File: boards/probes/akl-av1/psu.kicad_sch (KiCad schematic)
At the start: 15 parts, among them J1 U.FL, U1 LTC1983-5, U2 ADP7142ACPZN-R7, U3 ADP7182_DFN8

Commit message: Rev 0.2 of AKL-AV1
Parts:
- added L1: FERRITE, azonenberg_pcb:EIA_0402_CAP_NOSILK, symbol passive-azonenberg:INDUCTOR_PWROUT
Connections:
- net 5V0_N: now also L1.2; no longer C7.1, U1.2 (VOUT)
- new net: C7.1, L1.1, U1.2 (VOUT)
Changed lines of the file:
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@@
 (kicad_sch (version 20211123) (generator eeschema)
   (paper "A4")
+  (junction (at 72.39 26.67) (diameter 0) (color 0 0 0 0)
+  )
   (junction (at 34.29 99.06) (diameter 0) (color 0 0 0 0)
   )
@@
     (effects (font (size 1.27 1.27)) (justify left bottom))
   )
-  (label "5V0_N" (at 72.39 26.67 0)
+  (label "5V0_N" (at 87.63 26.67 0)
     (effects (font (size 1.27 1.27)) (justify left bottom))
   )
@@
     )
     (pin "1")
+    (pin "2")
+  )
+  (symbol (lib_id "passive-azonenberg:INDUCTOR_PWROUT") (at 80.01 26.67 90) (unit 1)
+    (in_bom yes) (on_board yes) (fields_autoplaced)
+    (property "Reference" "L1" (id 0) (at 80.01 22.1248 90)
+      (effects (font (size 1.016 1.016)))
+    )
+    (property "Value" "FERRITE" (id 1) (at 80.01 24.3956 90)
+      (effects (font (size 1.016 1.016)))
+    )
+    (property "Footprint" "azonenberg_pcb:EIA_0402_CAP_NOSILK" (id 2) (at 80.01 26.67 0)
+      (effects (font (size 1.524 1.524)) hide)
+    )
+    (property "Datasheet" "" (id 3) (at 80.01 26.67 0)
+      (effects (font (size 1.524 1.524)))
+    )
+    (pin "1")

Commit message: Updated AKL-AV1 design files for v0.3 prototype
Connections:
- net 5V0_N: now also L1.1; no longer L1.2
- net at C7.1, U1.2 (VOUT): now also L1.2; no longer L1.1
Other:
- moved on the sheet: L1
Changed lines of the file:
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@@
 (kicad_sch (version 20211123) (generator eeschema)
   (paper "A4")
+  (title_block
+    (date "2022-07-03")
+  )
   (junction (at 72.39 26.67) (diameter 0) (color 0 0 0 0)
   )
@@
     (pin "2")
   )
-  (symbol (lib_id "passive-azonenberg:INDUCTOR_PWROUT") (at 80.01 26.67 90) (unit 1)
-    (in_bom yes) (on_board yes) (fields_autoplaced)
-    (property "Reference" "L1" (id 0) (at 80.01 22.1248 90)
+  (symbol (lib_id "passive-azonenberg:INDUCTOR_PWROUT") (at 80.01 26.67 270) (unit 1)
+    (in_bom yes) (on_board yes) (fields_autoplaced)
+    (property "Reference" "L1" (id 0) (at 80.01 23.3952 90)
       (effects (font (size 1.016 1.016)))
     )
-    (property "Value" "FERRITE" (id 1) (at 80.01 24.3956 90)
+    (property "Value" "FERRITE" (id 1) (at 80.01 25.666 90)
       (effects (font (size 1.016 1.016)))
     )

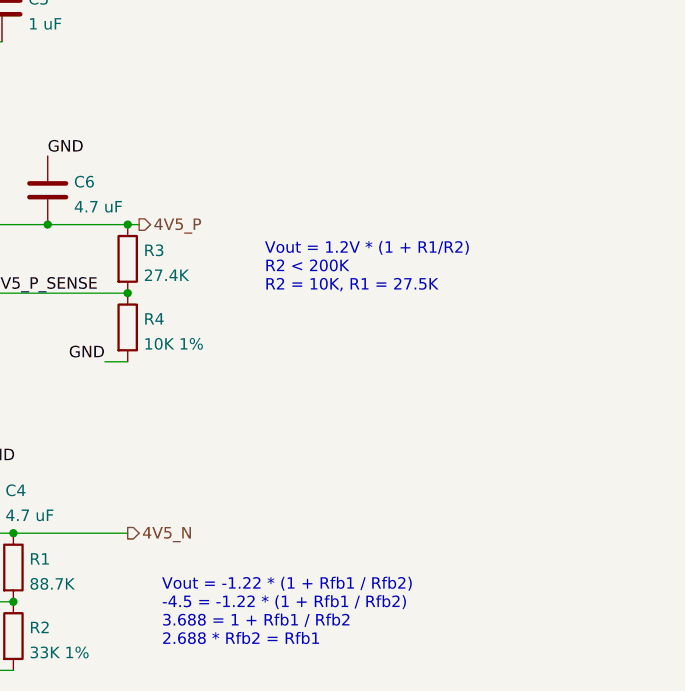
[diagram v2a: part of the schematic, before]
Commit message: Updated AKL-AV1 with v0.4 layout including OPA210 and noise filter
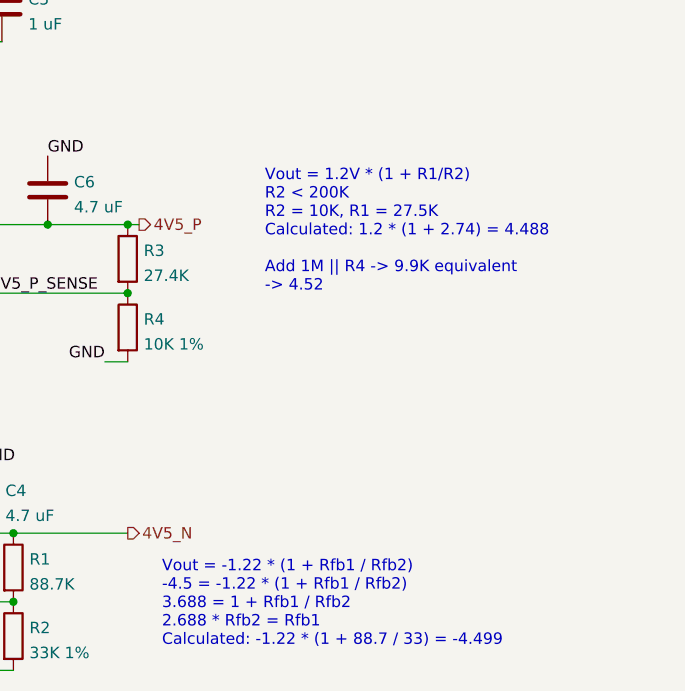
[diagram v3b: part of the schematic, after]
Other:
- note added: "Vout = -1.22 * (1 + Rfb1 / Rfb2) -4.5 = -1.22 * (1 + Rfb1 / Rfb2) 3.688 = 1 + Rfb1 / Rfb2 2.688 * Rfb2 = Rfb1 Calculated: -1.22 * (1 + 88.7 / 33) = -4.499"
- note added: "Vout = 1.2V * (1 + R1/R2) R2 < 200K R2 = 10K, R1 = 27.5K Calculated: 1.2 * (1 + 2.74) = 4.488 Add 1M || R4 -> 9.9K equivalent -> 4.52"
- note removed: "Vout = -1.22 * (1 + Rfb1 / Rfb2) -4.5 = -1.22 * (1 + Rfb1 / Rfb2) 3.688 = 1 + Rfb1 / Rfb2 2.688 * Rfb2 = Rfb1"
- note removed: "Vout = 1.2V * (1 + R1/R2) R2 < 200K R2 = 10K, R1 = 27.5K"
- company: (none) -> Antikernel Labs
- title: (none) -> AKL-AV1 High Impedance Active Voltage Probe
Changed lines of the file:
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@@
   (paper "A4")
   (title_block
-    (date "2022-07-03")
+    (title "AKL-AV1 High Impedance Active Voltage Probe")
+    (date "2022-07-16")
+    (rev "0.4")
+    (company "Antikernel Labs")
+    (comment 1 "Andrew D. Zonenberg")
   )
   (junction (at 72.39 26.67) (diameter 0) (color 0 0 0 0)
@@
     (stroke (width 0) (type default) (color 0 0 0 0))
   )
-  (text "Vout = 1.2V * (1 + R1/R2)\nR2 < 200K\nR2 = 10K, R1 = 27.5K"
+  (text "Vout = 1.2V * (1 + R1/R2)\nR2 < 200K\nR2 = 10K, R1 = 27.5K\nCalculated: 1.2 * (1 + 2.74) = 4.488\n\nAdd 1M || R4 -> 9.9K equivalent\n-> 4.52"
     (at 90.17 67.31 0)
     (effects (font (size 1.27 1.27)) (justify left bottom))
   )
-  (text "Vout = -1.22 * (1 + Rfb1 / Rfb2)\n-4.5 = -1.22 * (1 + Rfb1 / Rfb2)\n3.688 = 1 + Rfb1 / Rfb2\n2.688 * Rfb2 = Rfb1"
+  (text "Vout = -1.22 * (1 + Rfb1 / Rfb2)\n-4.5 = -1.22 * (1 + Rfb1 / Rfb2)\n3.688 = 1 + Rfb1 / Rfb2\n2.688 * Rfb2 = Rfb1\nCalculated: -1.22 * (1 + 88.7 / 33) = -4.499"
     (at 78.74 106.68 0)
     (effects (font (size 1.27 1.27)) (justify left bottom))

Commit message: Added file missed in last commit
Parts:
- removed C7: 22 uF, azonenberg_pcb:EIA_1210_CAP_NOSILK, symbol device:C
- removed L1: FERRITE, azonenberg_pcb:EIA_0402_CAP_NOSILK, symbol passive-azonenberg:INDUCTOR_PWROUT
- removed U1: LTC1983-5, azonenberg_pcb:SOT23_6, symbol power-azonenberg:LTC1983
- removed U3: ADP7182_DFN8, azonenberg_pcb:DFN_8_0.5MM_3x3MM, symbol power-azonenberg:ADP7182_DFN8
- added U1: LM27761, azonenberg_pcb:DFN_8_0.5MM_2x2MM, symbol power-azonenberg:LM27761
- C4: value 4.7 uF -> 1 uF
- C5: value 1 uF -> 4.7 uF
- R1: value 88.7K -> 255K
- R2: value 33K 1% -> 95.3K
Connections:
- net 5V0_N is gone; now on net GND: C2.1
- net 4V5_N: now also C5.1, U1.4 (VOUT); no longer C4.2
- net GND: now also C5.2, U1.2 (GND), U1.PAD (GND); no longer C2.2, C4.1
- net 4V5_N_FB: now reaches R1.2, R2.1
- net 4V5_N_FB: now also U1.5 (VFB)
- net 6V0 renamed 5V5
- net 5V5: now also U1.1 (VIN), U1.6 (EN)
- new net: C2.2, U1.3 (CPOUT)
- new net: C4.1, U1.7 (C1-)
- new net: C4.2, U1.8 (C1+)
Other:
- note added: "Vout = -1.22 * (R1+R2) / R2 Vout * R2 = -1.22 * (R1+R2) -4.5*R2 = -1.22*(R1+R2) 3.688*R2 = R1+R2 R1 = 2.688*R2 R2 > 50K"
- note removed: "Vout = -1.22 * (1 + Rfb1 / Rfb2) -4.5 = -1.22 * (1 + Rfb1 / Rfb2) 3.688 = 1 + Rfb1 / Rfb2 2.688 * Rfb2 = Rfb1 Calculated: -1.22 * (1 + 88.7 / 33) = -4.499"
